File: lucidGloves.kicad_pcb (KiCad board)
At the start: 2 copper layers, 0 parts

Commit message: Mostly lay out PCB
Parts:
- added D1: LED, LED_THT:LED_D5.0mm, F.Cu at (184.2, 97.5)
- added H3: MountingHole, MountingHole:MountingHole_3.2mm_M3, F.Cu at (193.0, 70.0)
- added H5: MountingHole, MountingHole:MountingHole_3.2mm_M3, F.Cu at (163.5, 70.0)
- added H6: MountingHole, MountingHole:MountingHole_3.2mm_M3, F.Cu at (164.0, 91.4)
- added J1: USB_C_Receptacle, Connector_USB:USB_C_Receptacle_Molex_105450-0101, F.Cu at (211.8, 95.9)
- added J10: Conn_01x05_Pin, Connector_PinHeader_2.54mm:PinHeader_1x05_P2.54mm_Vertical, F.Cu at (149.0, 68.6)
- added J11: Conn_01x05_Pin, Connector_PinHeader_2.54mm:PinHeader_1x05_P2.54mm_Vertical, F.Cu at (149.0, 53.3)
- added J12: Conn_01x19_Socket, Connector_PinSocket_2.54mm:PinSocket_1x19_P2.54mm_Vertical, F.Cu at (203.0, 53.4)
- added J13: Conn_01x05_Pin, Connector_PinHeader_2.54mm:PinHeader_1x05_P2.54mm_Horizontal, B.Cu at (196.6, 62.9)
- added J14: Conn_01x03_Pin, Connector_PinHeader_2.54mm:PinHeader_1x03_P2.54mm_Vertical, F.Cu at (214.5, 64.0)
- added J15: Conn_01x03_Pin, Connector_PinHeader_2.54mm:PinHeader_1x03_P2.54mm_Vertical, F.Cu at (214.5, 68.7)
- added J16: Conn_01x03_Pin, Connector_PinHeader_2.54mm:PinHeader_1x03_P2.54mm_Vertical, F.Cu at (214.5, 73.3)
- added J17: Conn_01x03_Pin, Connector_PinHeader_2.54mm:PinHeader_1x03_P2.54mm_Vertical, F.Cu at (214.6, 78.2)
- added J18: Conn_01x03_Pin, Connector_PinHeader_2.54mm:PinHeader_1x03_P2.54mm_Vertical, F.Cu at (214.5, 82.6)
- added J2: USB_C_Receptacle, Connector_USB:USB_C_Receptacle_Molex_105450-0101, F.Cu at (195.0, 96.0)
- added J3: Conn_01x05_Pin, Connector_PinHeader_2.54mm:PinHeader_1x05_P2.54mm_Vertical, F.Cu at (148.9, 99.5)
- added J4: Conn_01x05_Pin, Connector_PinHeader_2.54mm:PinHeader_1x05_P2.54mm_Vertical, F.Cu at (164.9, 99.5)
- added J5: Conn_01x05_Pin, Connector_PinHeader_2.54mm:PinHeader_1x05_P2.54mm_Horizontal, F.Cu at (161.4, 62.9)
- added J6: Conn_01x16_Pin, Connector_PinHeader_2.54mm:PinHeader_1x16_P2.54mm_Vertical, B.Cu at (156.0, 94.0)
- added J7: Conn_01x08_Pin, Connector_PinHeader_2.54mm:PinHeader_1x08_P2.54mm_Vertical, B.Cu at (172.0, 83.8)
- added J8: Conn_01x19_Socket, Connector_PinSocket_2.54mm:PinSocket_1x19_P2.54mm_Vertical, F.Cu at (179.5, 53.4)
- added J9: Conn_01x05_Pin, Connector_PinHeader_2.54mm:PinHeader_1x05_P2.54mm_Vertical, F.Cu at (149.0, 84.0)
- added R1: 5100Ω, Resistor_SMD:R_0603_1608Metric, F.Cu at (212.2, 89.9)
- added R2: 5100Ω, Resistor_SMD:R_0603_1608Metric, F.Cu at (195.8, 90.0)
- added R3: 270Ω, Resistor_SMD:R_0603_1608Metric, F.Cu at (183.5, 88.3)
- added SW1: SW_Push, Button_Switch_THT:SW_TH_Tactile_Omron_B3F-10xx, F.Cu at (208.8, 53.2)
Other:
- board text added: "ESP/sensor power"

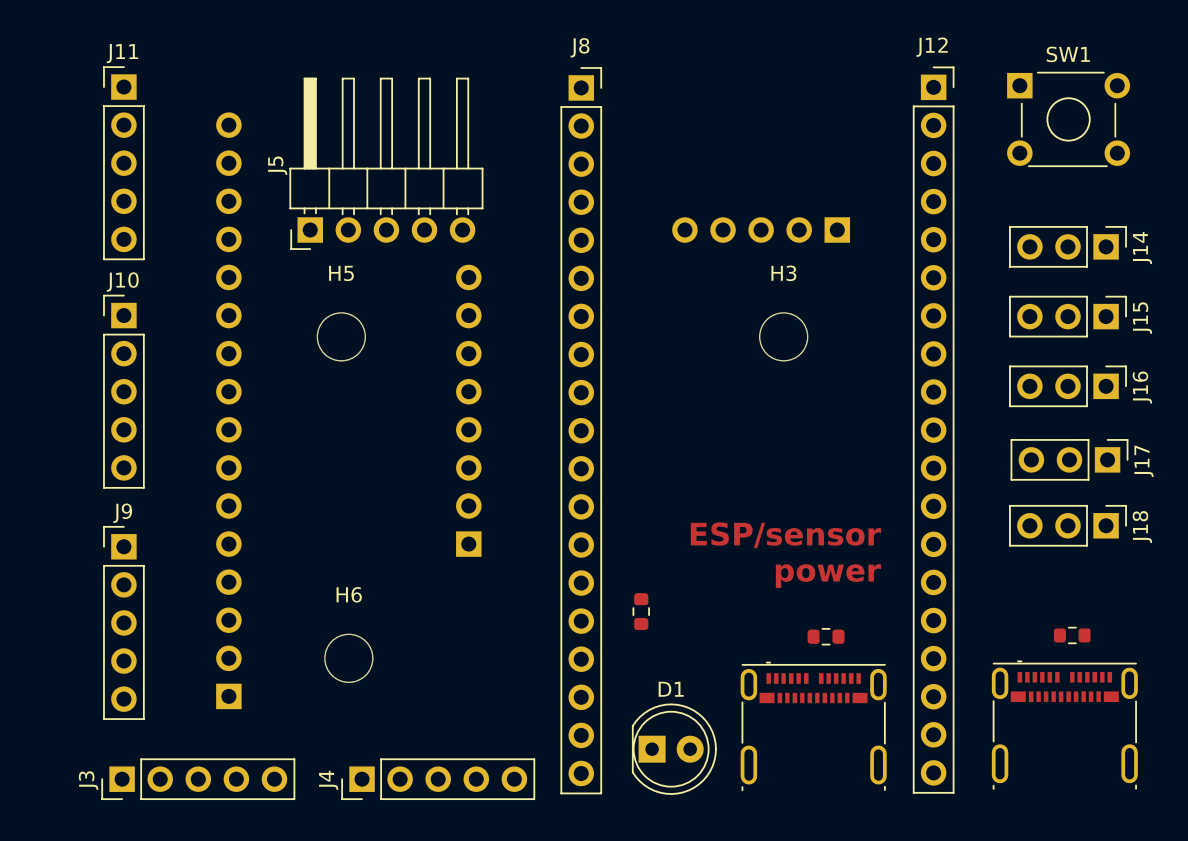
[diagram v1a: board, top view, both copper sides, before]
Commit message: Correct PCB alignment and spacing
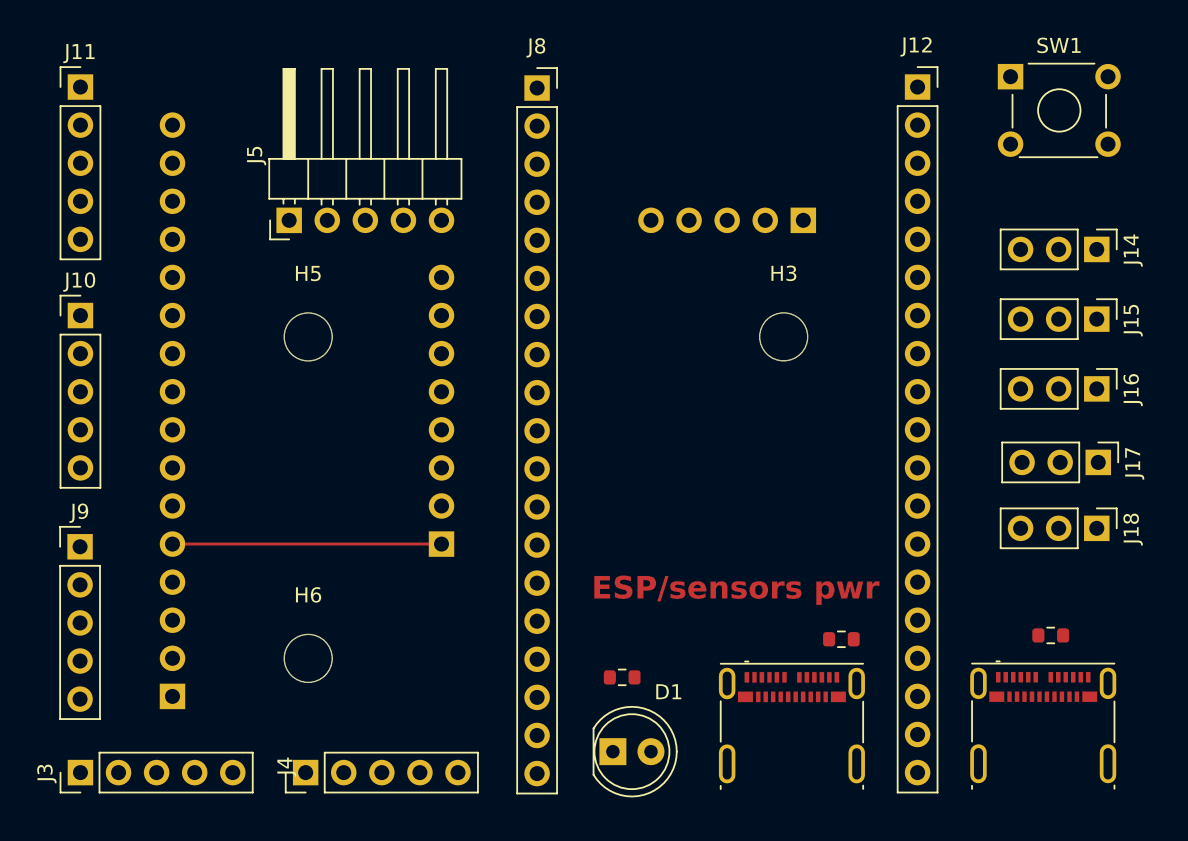
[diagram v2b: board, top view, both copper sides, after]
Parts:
- moved R3 4.57 mm to (182.2, 92.7), turned to 0 degrees
- moved J4 3.79 mm to (161.1, 99.1)
- moved J6 3.76 mm to (152.2, 94.0)
- moved J8 2.95 mm to (176.6, 53.4)
- moved J9 2.93 mm to (146.1, 84.0)
- moved J10 2.90 mm to (146.1, 68.6)
- moved J11 2.90 mm to (146.1, 53.3)
- moved J3 2.81 mm to (146.1, 99.1)
- moved H6 2.71 mm to (161.3, 91.4)
- moved D1 2.62 mm to (181.6, 97.7)
- moved J13 2.36 mm to (194.3, 62.2)
- moved H5 2.21 mm to (161.3, 70.0)
- moved J7 1.82 mm to (170.2, 83.8)
- moved J5 1.55 mm to (160.0, 62.2)
- moved J2 1.45 mm to (193.6, 95.9)
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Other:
- board text added: "ESP/sensors pwr"
- board text removed: "ESP/sensor power"

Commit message: Start routing wires and change USB C ports again
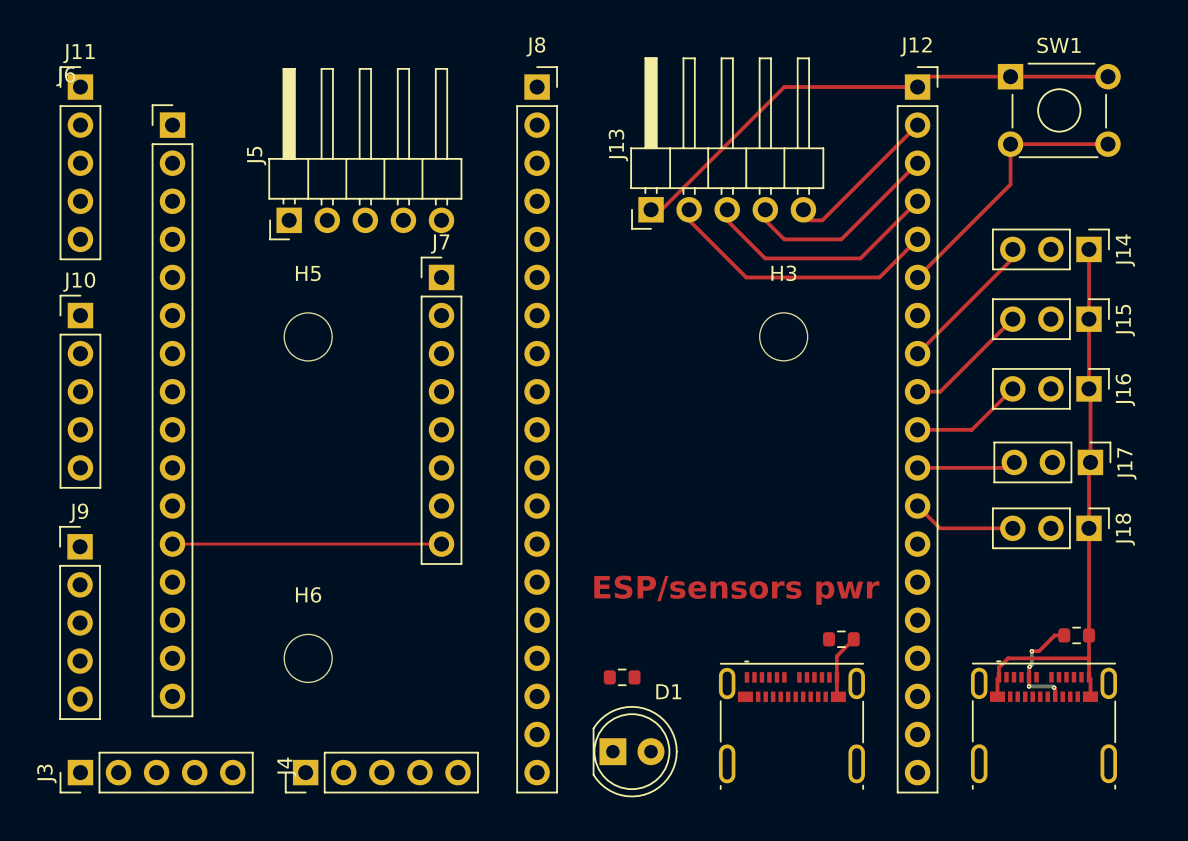
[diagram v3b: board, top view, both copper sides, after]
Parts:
- J13, J6, J7: moved to F.Cu
- moved J6 38.1 mm to (152.2, 55.9)
- moved J7 17.8 mm to (170.2, 66.0)
- moved J13 10.2 mm to (184.2, 61.5)
- moved R1 1.72 mm to (212.5, 89.9)
- moved J14 0.52 mm to (213.4, 64.2)
- moved J15 0.52 mm to (213.4, 68.8)
- moved J16 0.52 mm to (213.4, 73.5)
- moved J17 0.52 mm to (213.5, 78.4)
- moved J18 0.52 mm to (213.4, 82.8)
- moved J8 0.06 mm to (176.6, 53.3)
- moved J1 0.05 mm to (210.4, 95.9)
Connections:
- J10 pad 5: Net-(J10-Pin_5) -> Net-(J10-Pin_1)
- J11 pad 5: Net-(J10-Pin_5) -> Net-(J10-Pin_1)
- J13 pad 1: Net-(J12-Pin_2) -> Net-(J12-Pin_1)
- J13 pad 2: Net-(J12-Pin_3) -> Net-(J12-Pin_5)
- J13 pad 4: Net-(J12-Pin_5) -> Net-(J12-Pin_3)
- J13 pad 5: Net-(J12-Pin_1) -> Net-(J12-Pin_2)
- J2 pad A1: Net-(J10-Pin_5) -> Net-(J10-Pin_1)
- J2 pad A12: Net-(J10-Pin_5) -> Net-(J10-Pin_1)
- J2 pad B1: Net-(J10-Pin_5) -> Net-(J10-Pin_1)
- J2 pad B12: Net-(J10-Pin_5) -> Net-(J10-Pin_1)
- J3 pad 1: Net-(J10-Pin_5) -> Net-(J10-Pin_1)
- J4 pad 1: Net-(J10-Pin_5) -> Net-(J10-Pin_1)
- J5 pad 1: Net-(J10-Pin_5) -> Net-(J10-Pin_1)
- J6 pad 1: Net-(J4-Pin_4) -> Net-(J11-Pin_2)
- J6 pad 10: Net-(J10-Pin_2) -> Net-(J3-Pin_3)
- J6 pad 11: Net-(J10-Pin_4) -> Net-(J3-Pin_2)
- J6 pad 12: Net-(J10-Pin_3) -> Net-(J3-Pin_4)
- J6 pad 13: Net-(J11-Pin_3) -> Net-(J4-Pin_3)
- J6 pad 14: Net-(J11-Pin_4) -> Net-(J4-Pin_2)
- J6 pad 15: Net-(J11-Pin_2) -> Net-(J4-Pin_4)
- J6 pad 2: Net-(J4-Pin_2) -> Net-(J11-Pin_4)
- J6 pad 3: Net-(J4-Pin_3) -> Net-(J11-Pin_3)
- J6 pad 4: Net-(J3-Pin_4) -> Net-(J10-Pin_3)
- J6 pad 5: Net-(J3-Pin_2) -> Net-(J10-Pin_4)
- J6 pad 6: Net-(J3-Pin_3) -> Net-(J10-Pin_2)
- J7 pad 1: Net-(J7-Pin_1) -> Net-(J10-Pin_1)
- J7 pad 2: Net-(J7-Pin_2) -> unconnected-(J7-Pin_2-Pad2)
- J7 pad 6: unconnected-(J7-Pin_6-Pad6) -> Net-(J7-Pin_6)
- J7 pad 7: Net-(J10-Pin_1) -> Net-(J7-Pin_7)
- J7 pad 8: Net-(J10-Pin_5) -> unconnected-(J7-Pin_8-Pad8)
- J8 pad 10: Net-(J7-Pin_3) -> Net-(J7-Pin_5)
- J8 pad 11: Net-(J7-Pin_2) -> Net-(J7-Pin_6)
- J8 pad 14: Net-(J10-Pin_5) -> Net-(J10-Pin_1)
- J8 pad 3: Net-(J7-Pin_1) -> Net-(J7-Pin_7)
- J8 pad 8: Net-(J7-Pin_5) -> Net-(J7-Pin_3)
- J9 pad 2: Net-(J6-Pin_7) -> Net-(J6-Pin_9)
- J9 pad 3: Net-(J6-Pin_9) -> Net-(J6-Pin_7)
- J9 pad 5: Net-(J10-Pin_5) -> Net-(J10-Pin_1)
- R2 pad 2: Net-(J10-Pin_5) -> Net-(J10-Pin_1)
- R3 pad 1: Net-(J10-Pin_5) -> Net-(J10-Pin_1)
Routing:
- net Net-(J14-Pin_1): track 0.00 -> 38.2 mm
- net Net-(J12-Pin_1): track 0.00 -> 34.4 mm
- net Net-(J12-Pin_6): track 0.00 -> 18.0 mm
- net Net-(J12-Pin_5): track 0.00 -> 17.9 mm
- net Net-(J12-Pin_4): track 0.00 -> 15.3 mm
- net Net-(J12-Pin_3): track 0.00 -> 12.8 mm
- net Net-(J12-Pin_2): track 0.00 -> 10.3 mm
- net Net-(J12-Pin_8): track 0.00 -> 9.58 mm
- net Net-(J12-Pin_9): track 0.00 -> 8.35 mm
- net Net-(J12-Pin_10): track 0.00 -> 7.48 mm
- net Net-(J1-CC1): track 0.00 -> 7.37 mm, vias 0 -> 4
- net Net-(J12-Pin_12): track 0.00 -> 6.97 mm
- net Net-(J12-Pin_11): track 0.00 -> 6.60 mm
- net Net-(J10-Pin_1): track 0.00 -> 4.35 mm

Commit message: Finish PCB
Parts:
- removed J2: USB_C_Receptacle, Connector_USB:USB_C_Receptacle_Molex_105450-0101
- added J19: USB_C_Receptacle_PowerOnly_6P, Connector_USB:USB_C_Receptacle_GCT_USB4135-GF-A_6P_TopMnt_Horizontal, F.Cu at (193.0, 96.5)
- J1: value USB_C_Receptacle -> USB_C_Receptacle_PowerOnly_6P; footprint Connector_USB:USB_C_Receptacle_Molex_105450-0101 -> Connector_USB:USB_C_Receptacle_GCT_USB4135-GF-A_6P_TopMnt_Horizontal
- moved R2 2.09 mm to (194.8, 90.2)
- moved D1 1.08 mm to (180.5, 97.6)
- moved J18 1.05 mm to (213.4, 83.8)
- moved J1 0.62 mm to (210.8, 96.3)
- moved R3 0.37 mm to (182.3, 92.4), turned to -90 degrees
- moved J17 0.10 mm to (213.4, 78.4)
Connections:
- J10 pad 5: Net-(J10-Pin_1) -> Net-(J10-Pin_5)
- J11 pad 5: Net-(J10-Pin_1) -> Net-(J10-Pin_5)
- J3 pad 1: Net-(J10-Pin_1) -> Net-(J10-Pin_5)
- J4 pad 1: Net-(J10-Pin_1) -> Net-(J10-Pin_5)
- J5 pad 1: Net-(J10-Pin_1) -> Net-(J10-Pin_5)
- J7 pad 1: Net-(J10-Pin_1) -> Net-(J10-Pin_5)
- J7 pad 2: unconnected-(J7-Pin_2-Pad2) -> Net-(J10-Pin_1)
- J7 pad 3: Net-(J7-Pin_3) -> unconnected-(J7-Pin_3-Pad3)
- J7 pad 8: unconnected-(J7-Pin_8-Pad8) -> Net-(J7-Pin_8)
- J8 pad 10: Net-(J7-Pin_5) -> Net-(J7-Pin_6)
- J8 pad 11: Net-(J7-Pin_6) -> Net-(J7-Pin_7)
- J8 pad 14: Net-(J10-Pin_1) -> Net-(J10-Pin_5)
- J8 pad 3: Net-(J7-Pin_7) -> Net-(J7-Pin_8)
- J8 pad 8: Net-(J7-Pin_3) -> Net-(J7-Pin_4)
- J8 pad 9: Net-(J7-Pin_4) -> Net-(J7-Pin_5)
- J9 pad 5: Net-(J10-Pin_1) -> Net-(J10-Pin_5)
- R2 pad 2: Net-(J10-Pin_1) -> Net-(J10-Pin_5)
- R3 pad 1: Net-(J10-Pin_1) -> Net-(J10-Pin_5)
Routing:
- net Net-(J10-Pin_5): track 0.00 -> 150.8 mm
- net Net-(J10-Pin_1): track 4.35 -> 120.7 mm
- net Net-(J14-Pin_2): track 0.00 -> 34.3 mm
- net Net-(J7-Pin_8): track 0.00 -> 28.0 mm
- net Net-(J6-Pin_9): track 0.00 -> 26.9 mm
- net Net-(J8-Pin_19): track 0.00 -> 23.6 mm, vias 0 -> 1
- net Net-(J3-Pin_3): track 0.00 -> 22.7 mm
- net Net-(J4-Pin_4): track 0.00 -> 21.3 mm
- net Net-(J6-Pin_8): track 0.00 -> 20.5 mm
- net Net-(J6-Pin_7): track 0.00 -> 20.5 mm
- net Net-(J3-Pin_2): track 0.00 -> 19.3 mm
- net Net-(J4-Pin_3): track 0.00 -> 19.2 mm
- net Net-(J10-Pin_2): track 0.00 -> 19.1 mm
- net Net-(J3-Pin_4): track 0.00 -> 16.8 mm
- net Net-(J4-Pin_2): track 0.00 -> 15.6 mm
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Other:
- board outline added: 73.7 x 50.8 mm
- board text added: "ESP/sensor power"
- board text added: "Servo power"
- board text removed: "ESP/sensors pwr"

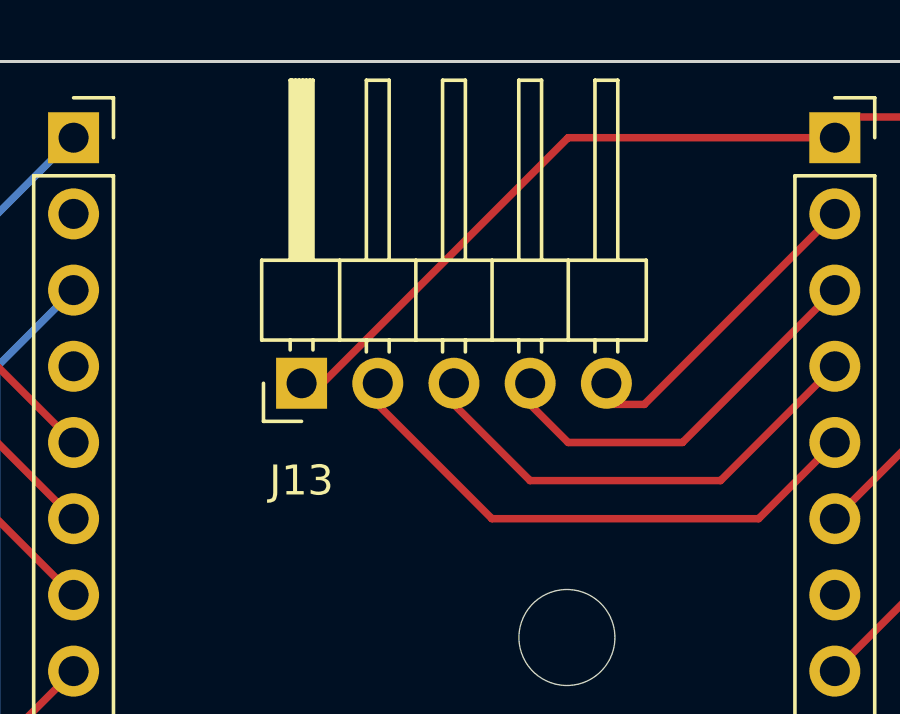
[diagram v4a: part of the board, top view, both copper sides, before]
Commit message: Fix tiny placement issue
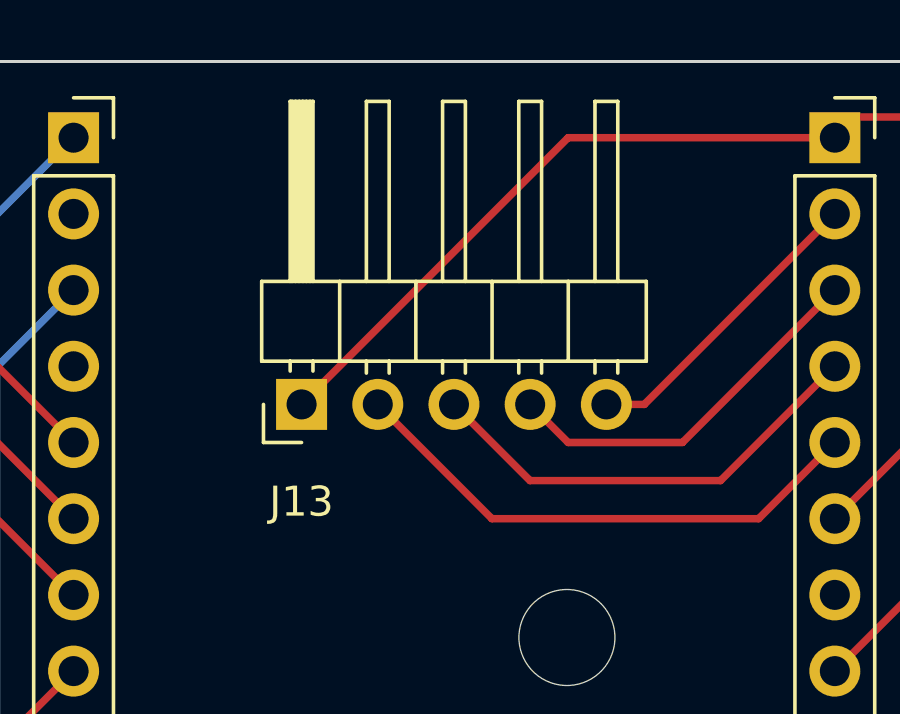
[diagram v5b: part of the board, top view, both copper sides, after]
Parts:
- moved J13 0.70 mm to (184.2, 62.2)
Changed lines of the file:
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@@
 	(footprint "Connector_PinHeader_2.54mm:PinHeader_1x05_P2.54mm_Horizontal"
 		(layer "F.Cu")
-		(at 184.155 61.525 90)
+		(at 184.155 62.23 90)
 		(descr "Through hole angled pin header, 1x05, 2.54mm pitch, 6mm pin length, single row")
 		(tags "Through hole angled pin header THT 1x05 2.54mm single row")

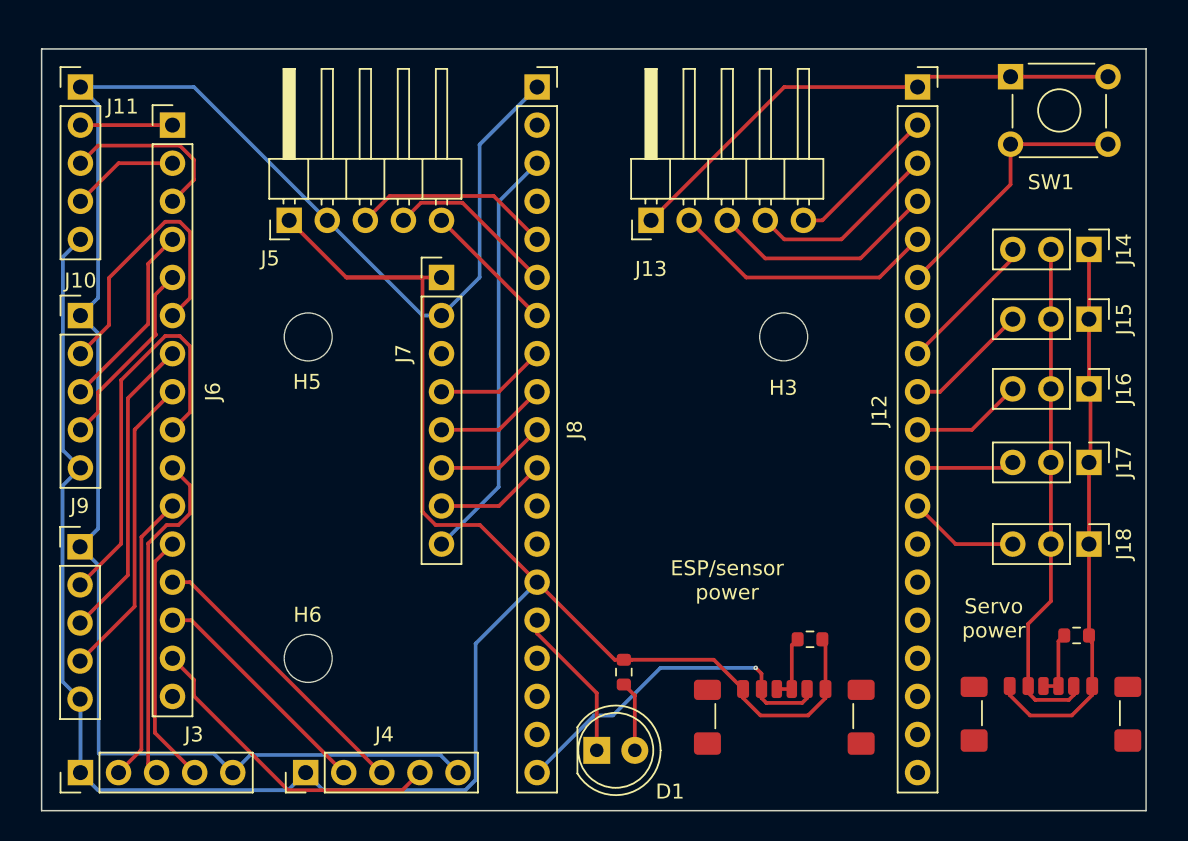
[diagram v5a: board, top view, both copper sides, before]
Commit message: Added servo/sensor labels and LucidVR logo
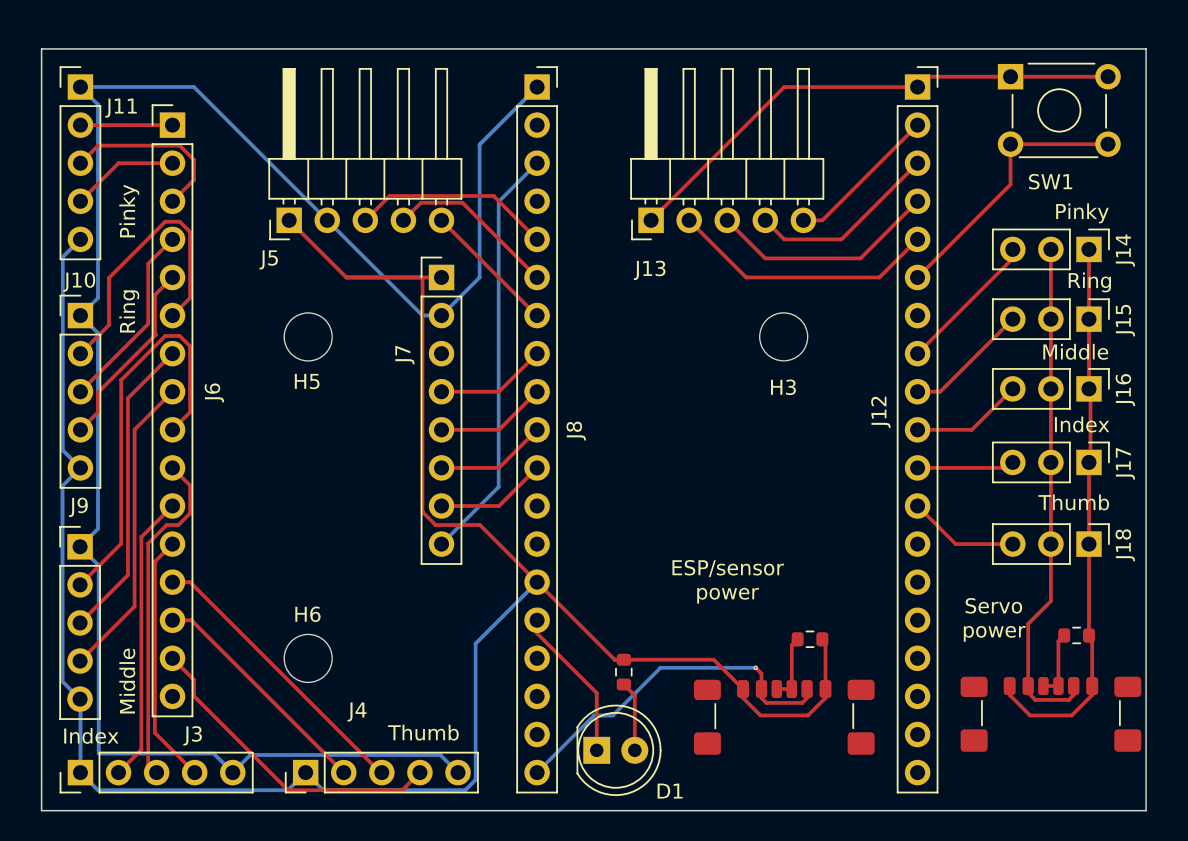
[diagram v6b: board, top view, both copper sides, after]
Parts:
- added G***: LOGO, LOGO, B.Cu at (188.0, 78.7)
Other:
- board text added: "Index"
- board text added: "Middle"
- board text added: "Pinky"
- board text added: "Ring"
- board text added: "Thumb"
